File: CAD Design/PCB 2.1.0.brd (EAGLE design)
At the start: 50 x 40 mm, 49 parts, among them U1 CC2538, U2 MAX1555, X1 32MHz, X2 FC-12M

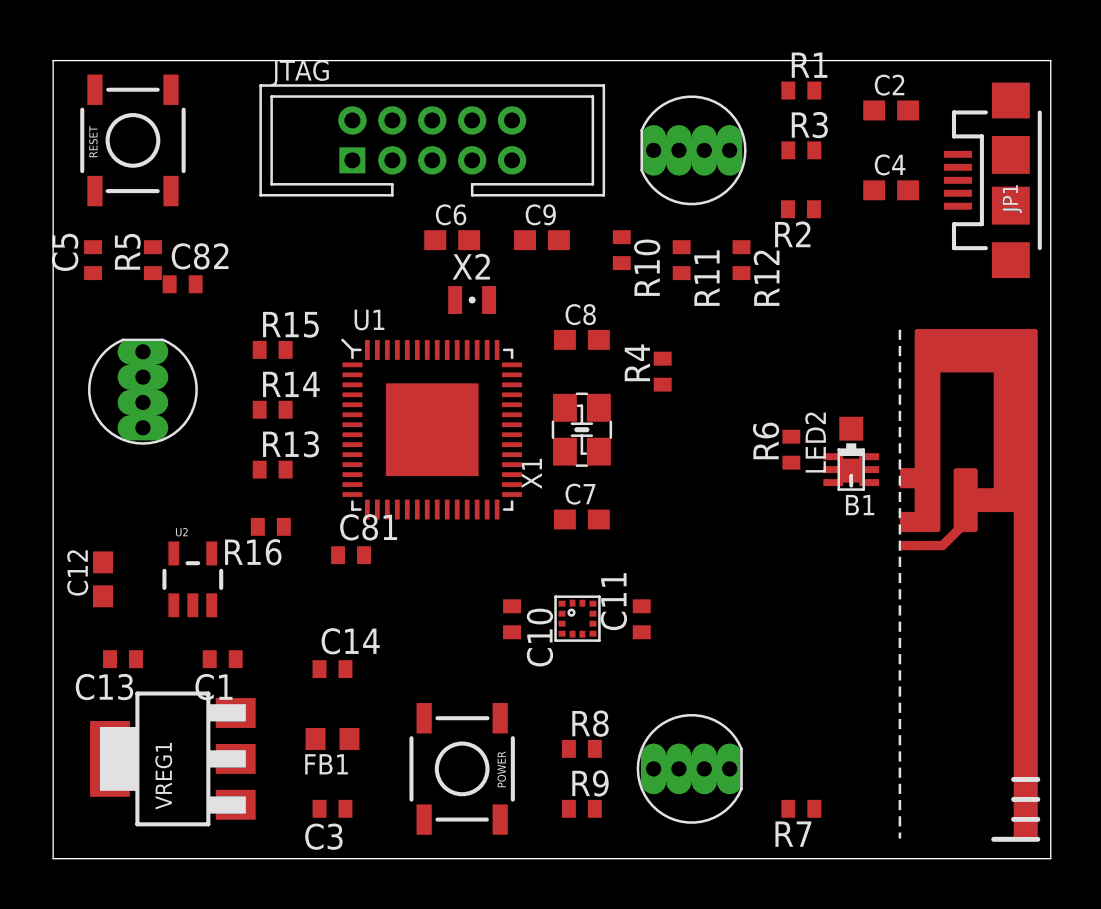
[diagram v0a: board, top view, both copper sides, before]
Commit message: Board update
Added Vbatt pads, ground plane, ready to route
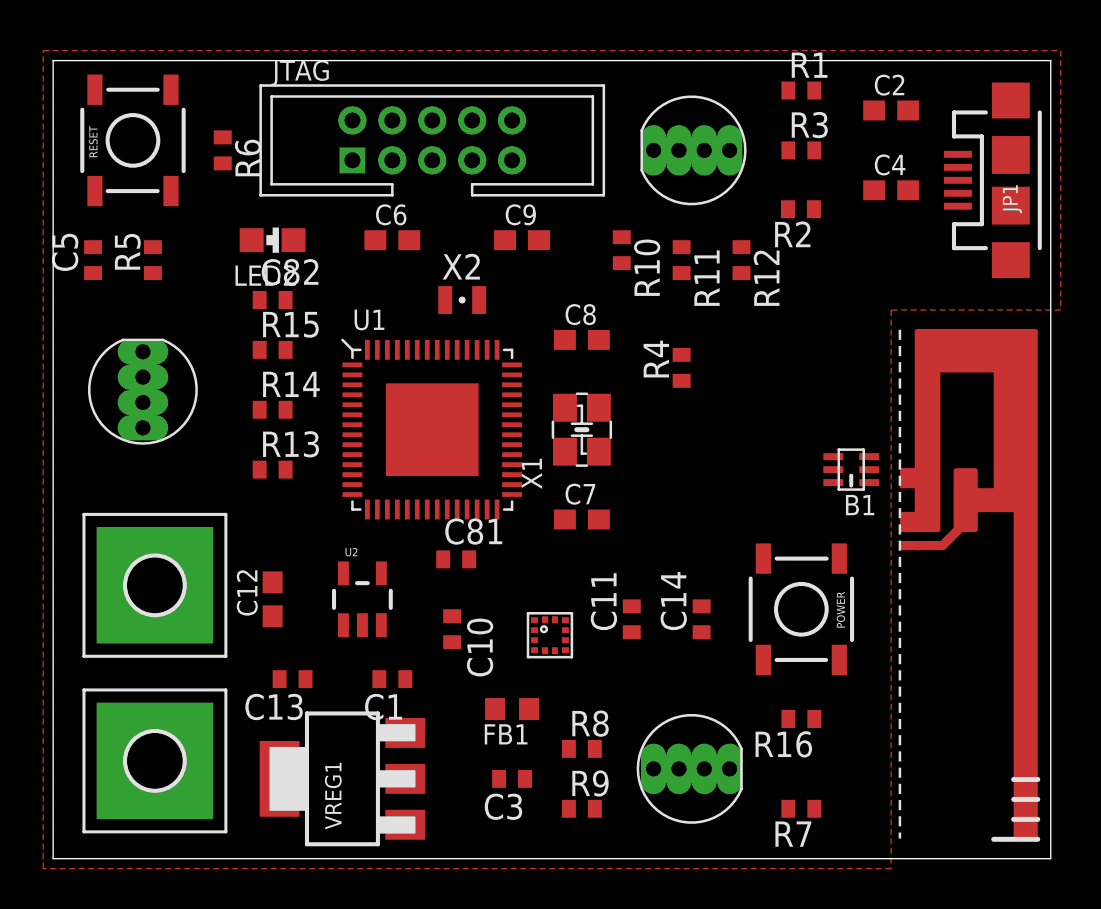
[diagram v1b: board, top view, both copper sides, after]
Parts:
- added H1, H2: MOUNT-PAD-SQUARE2.8, holes:2,8-PAD-SQUARE
- moved R6 32.2 mm to (8.50, 35.5), turned to 270 degrees
- moved LED2 30.8 mm to (11.0, 31.0), turned to 90 degrees
- moved R16 28.3 mm to (37.5, 7.00)
- moved POWER 18.8 mm to (37.5, 12.5)
- moved C14 18.7 mm to (32.5, 12.0), turned to 90 degrees
- moved C3 9.12 mm to (23.0, 4.00)
- moved FB1 9.12 mm to (23.0, 7.50)
- moved C1 8.56 mm to (17.0, 9.00)
- moved C12 8.56 mm to (11.0, 13.0)
- moved C13 8.56 mm to (12.0, 9.00)
- moved U2 8.56 mm to (15.5, 13.0)
- moved VREG1 8.56 mm to (14.5, 4.00)
- moved C81 5.27 mm to (20.2, 15.0)
- moved C82 4.58 mm to (11.0, 28.0)
- moved C10 3.04 mm to (20.0, 11.5)
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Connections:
- net GND: now also H2.B2,8
- net N$14: now also H1.B2,8
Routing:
- added copper zone on layer 1, net GND
